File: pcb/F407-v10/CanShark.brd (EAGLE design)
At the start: 97 x 80 mm, 129 parts, among them IC1 STM32F407V, IC2 KSZ8051MLL, K2 JACK_POWER_2,1, U1 SN65HVD230DR, U2 SN65HVD230DR, U3 LM2594M-ADJ, U4 LM2594M-ADJ, U5 TSH24IDT, U6 MCP602-E/SN

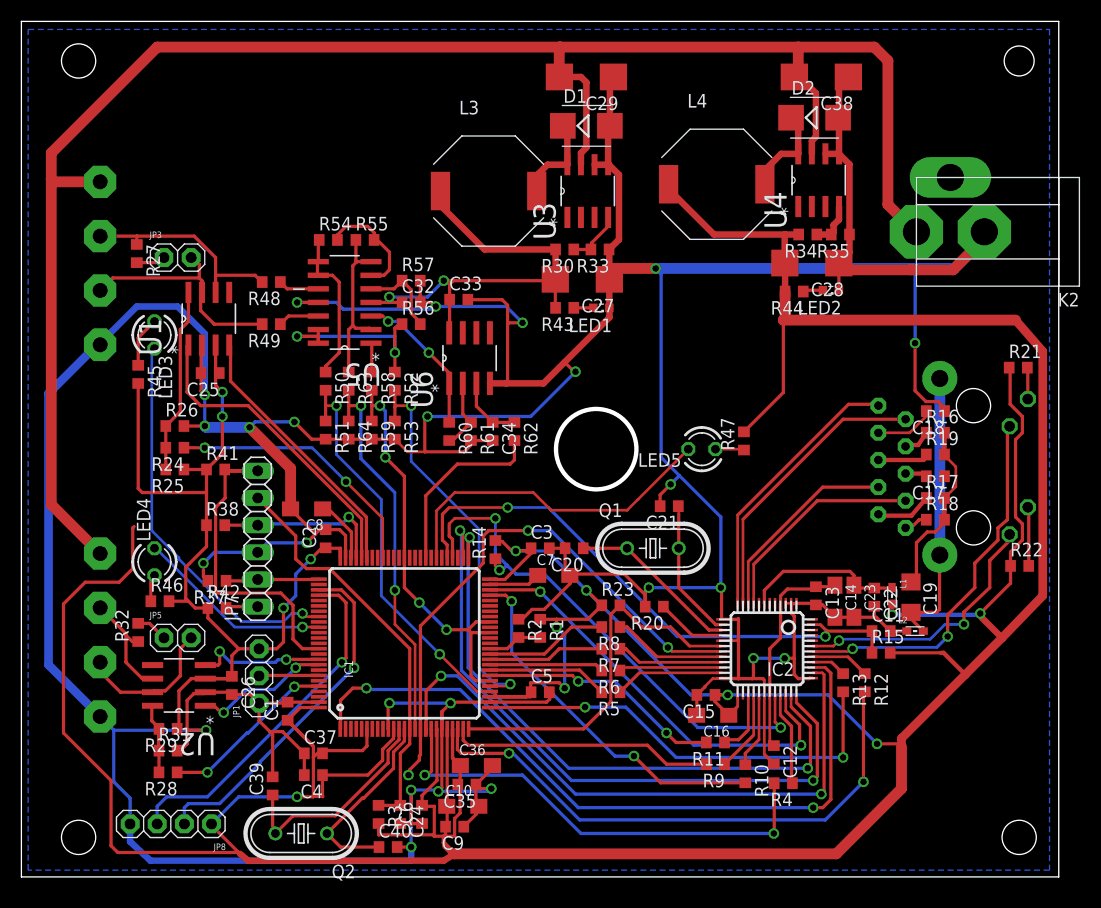
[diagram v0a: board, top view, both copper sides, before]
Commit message: [pcb] change mounting hole position, increase the isolation gap
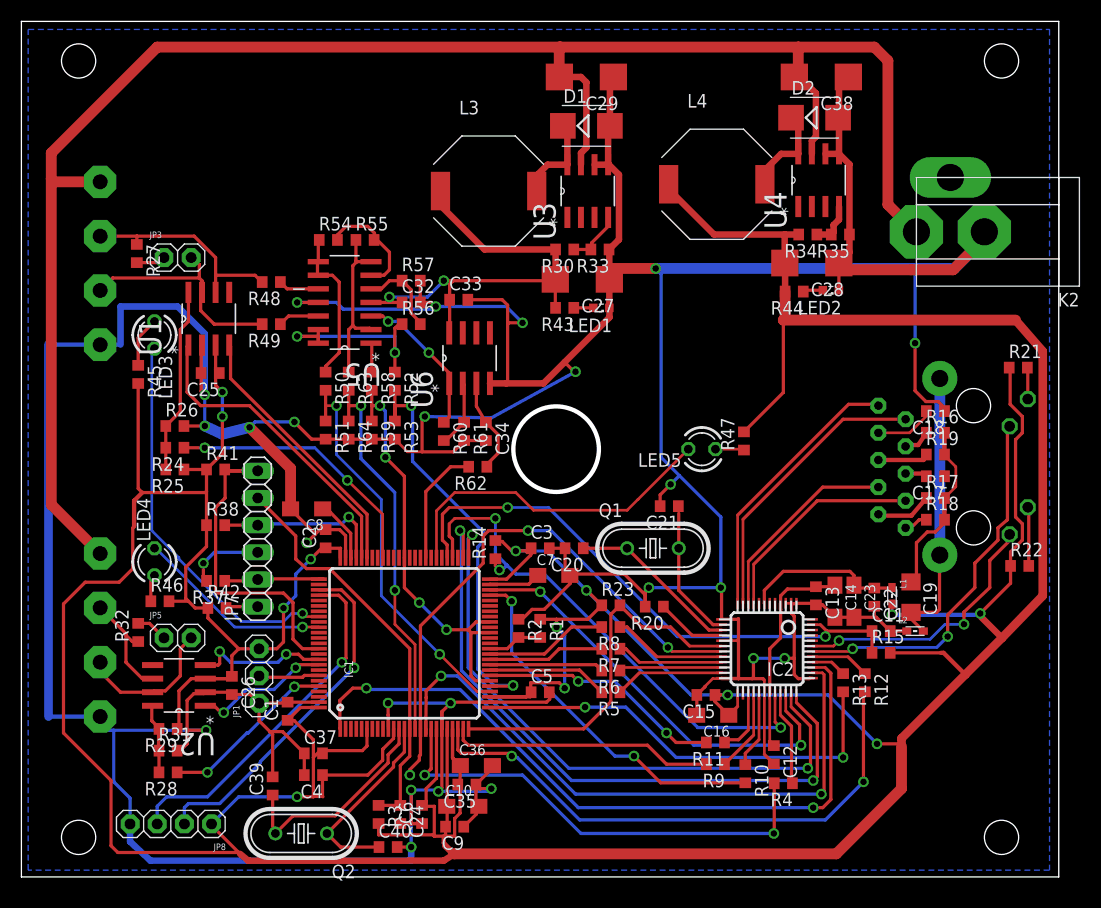
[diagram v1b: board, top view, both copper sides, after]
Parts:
- moved R62 4.76 mm to (42.7, 38.4), turned to 180 degrees
- moved C34 0.64 mm to (43.4, 41.7)
- moved R61 0.63 mm to (41.4, 41.7)
- moved R60 0.51 mm to (39.5, 41.7)
- moved R37 0.13 mm to (18.2, 27.7)
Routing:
- net ADC_TRIG_VALUE_PWM: track 17.3 -> 11.2 mm
- net N$71: track 6.31 -> 8.95 mm
- net ADC_CAN1H: track 37.1 -> 39.6 mm
- net JTG-TCK/SWCLK: track 8.74 -> 9.71 mm
- net CAN1_RX: track 26.0 -> 25.3 mm
- net GND: track 586.4 -> 587.1 mm
- net ETH_MII_TXD0: track 57.6 -> 58.3 mm
- net +3V3: track 535.7 -> 536.4 mm
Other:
- outline, holes or cut-outs redrawn

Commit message: [pcb] change texts of PCB
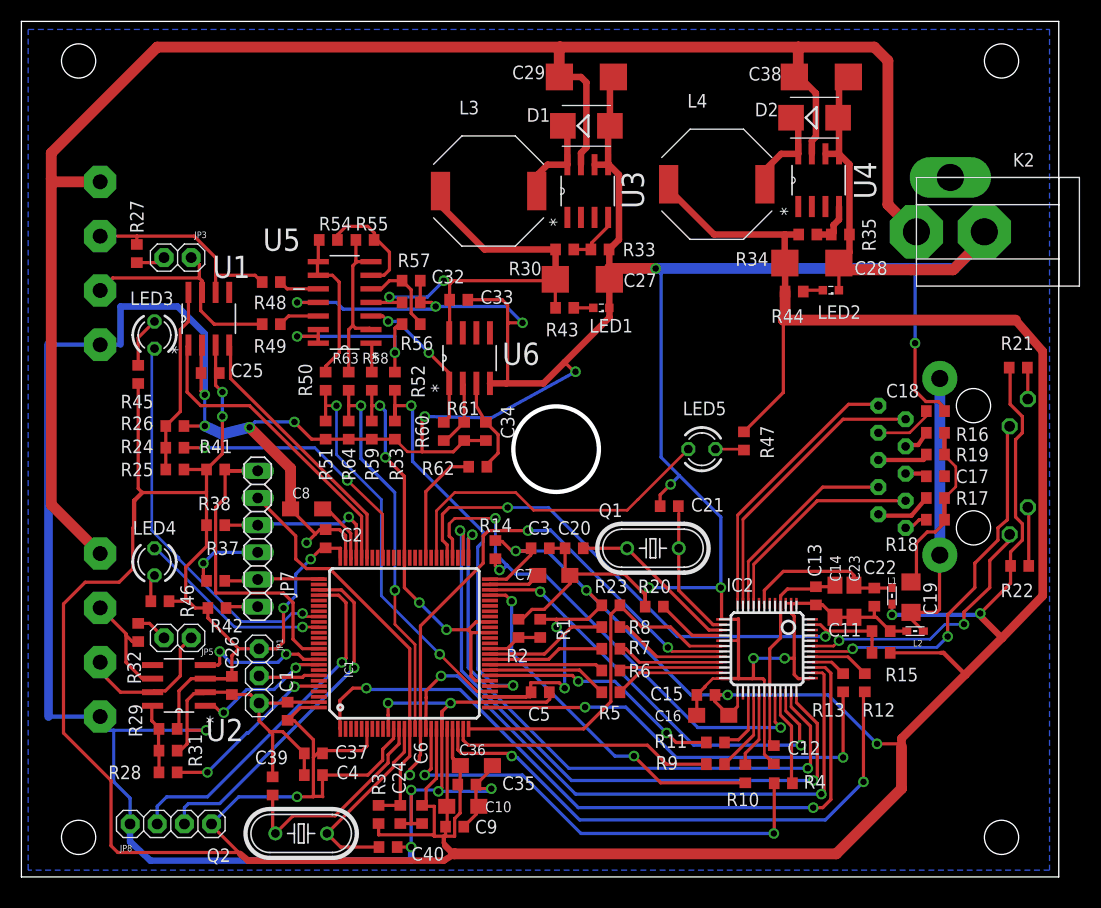
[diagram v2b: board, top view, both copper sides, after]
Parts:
- C27, C28: value (none) -> 100uF/16V
- C29, C38: value (none) -> 100uF/20V
- C35, C9: value 10nF -> 100nF
- D1, D2: value (none) -> SK26A
- L3: value (none) -> 68uH
- L4: value (none) -> 100uH
- R59: value 200k -> 100k
